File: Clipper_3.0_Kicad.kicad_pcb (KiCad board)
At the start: 2 copper layers, 19 parts, among them J10 Conn_01x19_Socket, J11 Screw_Terminal_01x02, J12 Conn_01x01_Socket, J13 Conn_01x01_Socket, J14 Conn_01x01_Socket, J15 Conn_01x01_Socket, J4 Conn_01x08_Socket, J5 Conn_01x08_Socket, J6 Conn_01x08_Socket, J9 Conn_01x19_Socket, U1 ESP32-DevKitC, U2 TB6612FNG_MODULE, U3 GY-521 MODULE, U4 DC/DC MINI-360

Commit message: Actualizacion de avance en SCH
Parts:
- removed REF**: TerminalBlock_Xinya_XY308-2.54-19P_1x19_P2.54mm_Horizontal, TerminalBlock:TerminalBlock_Xinya_XY308-2.54-19P_1x19_P2.54mm_Horizontal
- removed REF**: CP_Radial_D8.0mm_P3.50mm, Capacitor_THT:CP_Radial_D8.0mm_P3.50mm
- removed REF** (x2): TerminalBlock_Xinya_XY308-2.54-2P_1x02_P2.54mm_Horizontal, TerminalBlock:TerminalBlock_Xinya_XY308-2.54-2P_1x02_P2.54mm_Horizontal
- removed REF**: SOT-223-3_TabPin2, Package_TO_SOT_SMD:SOT-223-3_TabPin2
- added C1: C_Polarized_Small, Capacitor_THT:CP_Radial_D8.0mm_P3.50mm, F.Cu at (161.4, 65.0)
- added J20: Screw_Terminal_01x02, TerminalBlock:TerminalBlock_Xinya_XY308-2.54-2P_1x02_P2.54mm_Horizontal, F.Cu at (186.6, 63.7)
- added J21: Screw_Terminal_01x16, TerminalBlock:TerminalBlock_Xinya_XY308-2.54-16P_1x16_P2.54mm_Horizontal, F.Cu at (113.4, 76.1)
- added R1: 3.3K, Resistor_SMD:R_1206_3216Metric_Pad1.30x1.75mm_HandSolder, B.Cu at (122.2, 109.2)
- added R2: 4.7K, Resistor_SMD:R_1206_3216Metric_Pad1.30x1.75mm_HandSolder, B.Cu at (122.2, 111.9)
- added R3: 3.3V, Resistor_SMD:R_1206_3216Metric_Pad1.30x1.75mm_HandSolder, B.Cu at (147.9, 94.7)
- added R4: 4.7K, Resistor_SMD:R_1206_3216Metric_Pad1.30x1.75mm_HandSolder, B.Cu at (147.8, 98.0)
- U5: renamed from U1; value ESP32-DevKitC -> AMS1117-3.3; footprint Espressif:ESP32-DevKitC -> Package_TO_SOT_SMD:SOT-223-3_TabPin2; moved to B.Cu
- moved U5 64.7 mm to (164.5, 131.2)
- moved J10 50.0 mm to (127.8, 119.1), turned to 180 degrees
- moved J9 48.5 mm to (153.2, 119.1), turned to 180 degrees
- moved J11 18.7 mm to (184.0, 133.5)
- moved J6 17.8 mm to (170.6, 103.7), turned to 90 degrees
- moved J4 0.22 mm to (188.8, 86.6)
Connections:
- J10 pad 1: unconnected-(J10-Pin_1-Pad1) -> GND
- J10 pad 11: unconnected-(J10-Pin_11-Pad11) -> S1
- J10 pad 12: unconnected-(J10-Pin_12-Pad12) -> S0
- J10 pad 13: unconnected-(J10-Pin_13-Pad13) -> SIG
- J10 pad 17: unconnected-(J10-Pin_17-Pad17) -> Net-(J10-Pin_17)
- J10 pad 18: unconnected-(J10-Pin_18-Pad18) -> /LED
- J10 pad 19: unconnected-(J10-Pin_19-Pad19) -> /BTN
- J10 pad 2: unconnected-(J10-Pin_2-Pad2) -> Net-(J10-Pin_2)
- J10 pad 3: unconnected-(J10-Pin_3-Pad3) -> Net-(J10-Pin_3)
- J10 pad 6: unconnected-(J10-Pin_6-Pad6) -> Net-(J10-Pin_6)
- J10 pad 7: unconnected-(J10-Pin_7-Pad7) -> GND
- J10 pad 8: unconnected-(J10-Pin_8-Pad8) -> S3
- J10 pad 9: unconnected-(J10-Pin_9-Pad9) -> S2
- J11 pad 1: unconnected-(J11-Pin_1-Pad1) -> /BO2
- J11 pad 2: unconnected-(J11-Pin_2-Pad2) -> /BO1
- J12 pad 1: unconnected-(J12-Pin_1-Pad1) -> VCC12V
- J13 pad 1: unconnected-(J13-Pin_1-Pad1) -> GND
- J14 pad 1: unconnected-(J14-Pin_1-Pad1) -> VCC5V
- J15 pad 1: unconnected-(J15-Pin_1-Pad1) -> GND
- J5 pad 1: /VM -> VCC12V
- J5 pad 2: /VCC -> VCC3.3V
- J6 pad 1: unconnected-(J6-Pin_1-Pad1) -> VCC3.3V
- J6 pad 2: unconnected-(J6-Pin_2-Pad2) -> GND
- J6 pad 3: unconnected-(J6-Pin_3-Pad3) -> Net-(J10-Pin_3)
- J6 pad 4: unconnected-(J6-Pin_4-Pad4) -> Net-(J10-Pin_6)
- J9 pad 10: unconnected-(J9-Pin_10-Pad10) -> /BIN1
- J9 pad 11: unconnected-(J9-Pin_11-Pad11) -> /STBY
- J9 pad 12: unconnected-(J9-Pin_12-Pad12) -> /AIN1
- J9 pad 13: unconnected-(J9-Pin_13-Pad13) -> /AIN2
- J9 pad 14: unconnected-(J9-Pin_14-Pad14) -> GND
- J9 pad 15: unconnected-(J9-Pin_15-Pad15) -> /PWMA
- J9 pad 19: unconnected-(J9-Pin_19-Pad19) -> VCC5V
- J9 pad 7: unconnected-(J9-Pin_7-Pad7) -> Net-(J9-Pin_7)
- J9 pad 8: unconnected-(J9-Pin_8-Pad8) -> /PWMB
- J9 pad 9: unconnected-(J9-Pin_9-Pad9) -> /BIN2
- U5 pad 1: unconnected-(U1-3V3-Pad1) -> GND
- U5 pad 2: unconnected-(U1-CHIP_PU-Pad2) -> VCC3.3V
- U5 pad 3: unconnected-(U1-SENSOR_VP/GPIO36/ADC1_CH0-Pad3) -> VCC5V
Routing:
- net VCC3.3V: track 0.00 -> 191.0 mm
- net VCC5V: track 0.00 -> 158.0 mm
- net unconnected-(U4-VCC_In-Pad1): track 151.1 -> 0.00 mm, vias 2 -> 0
- net VCC12V: track 0.00 -> 149.7 mm
- net /BO2: track 0.00 -> 120.2 mm
- net Net-(J2-Pin_7): track 120.0 -> 0.00 mm
- net Net-(J2-Pin_6): track 106.0 -> 0.00 mm
- net unconnected-(U3-VCC-Pad1): track 105.8 -> 0.00 mm
- net /BO1: track 0.00 -> 105.7 mm
- net Net-(J10-Pin_6): track 0.00 -> 89.3 mm
- net Net-(J10-Pin_3): track 0.00 -> 79.7 mm
- net Net-(J2-Pin_2): track 66.1 -> 0.00 mm
- net /ENCD: track 0.00 -> 62.3 mm
- net /PWMA: track 0.00 -> 44.2 mm
- net GND: track 22.5 -> 66.6 mm, vias 5 -> 7
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
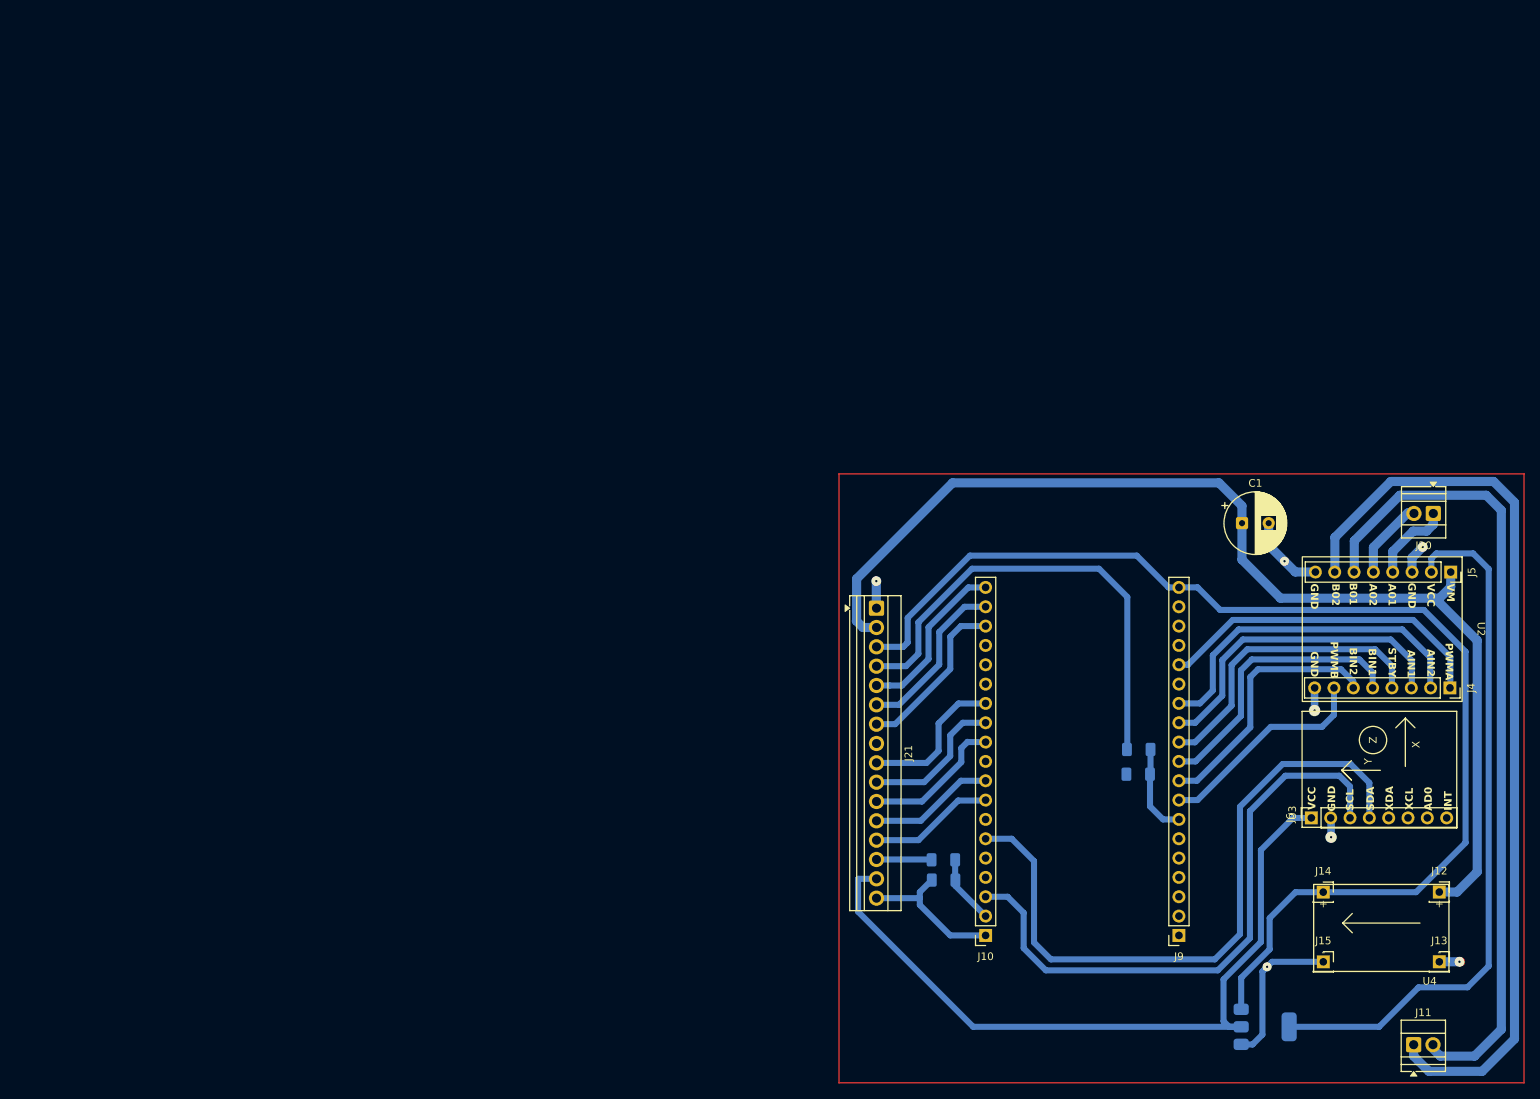
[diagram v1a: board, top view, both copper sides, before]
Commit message: Terminacion del equematico y redistribucion de pines del ESP32 para evitar conflicto con wifi
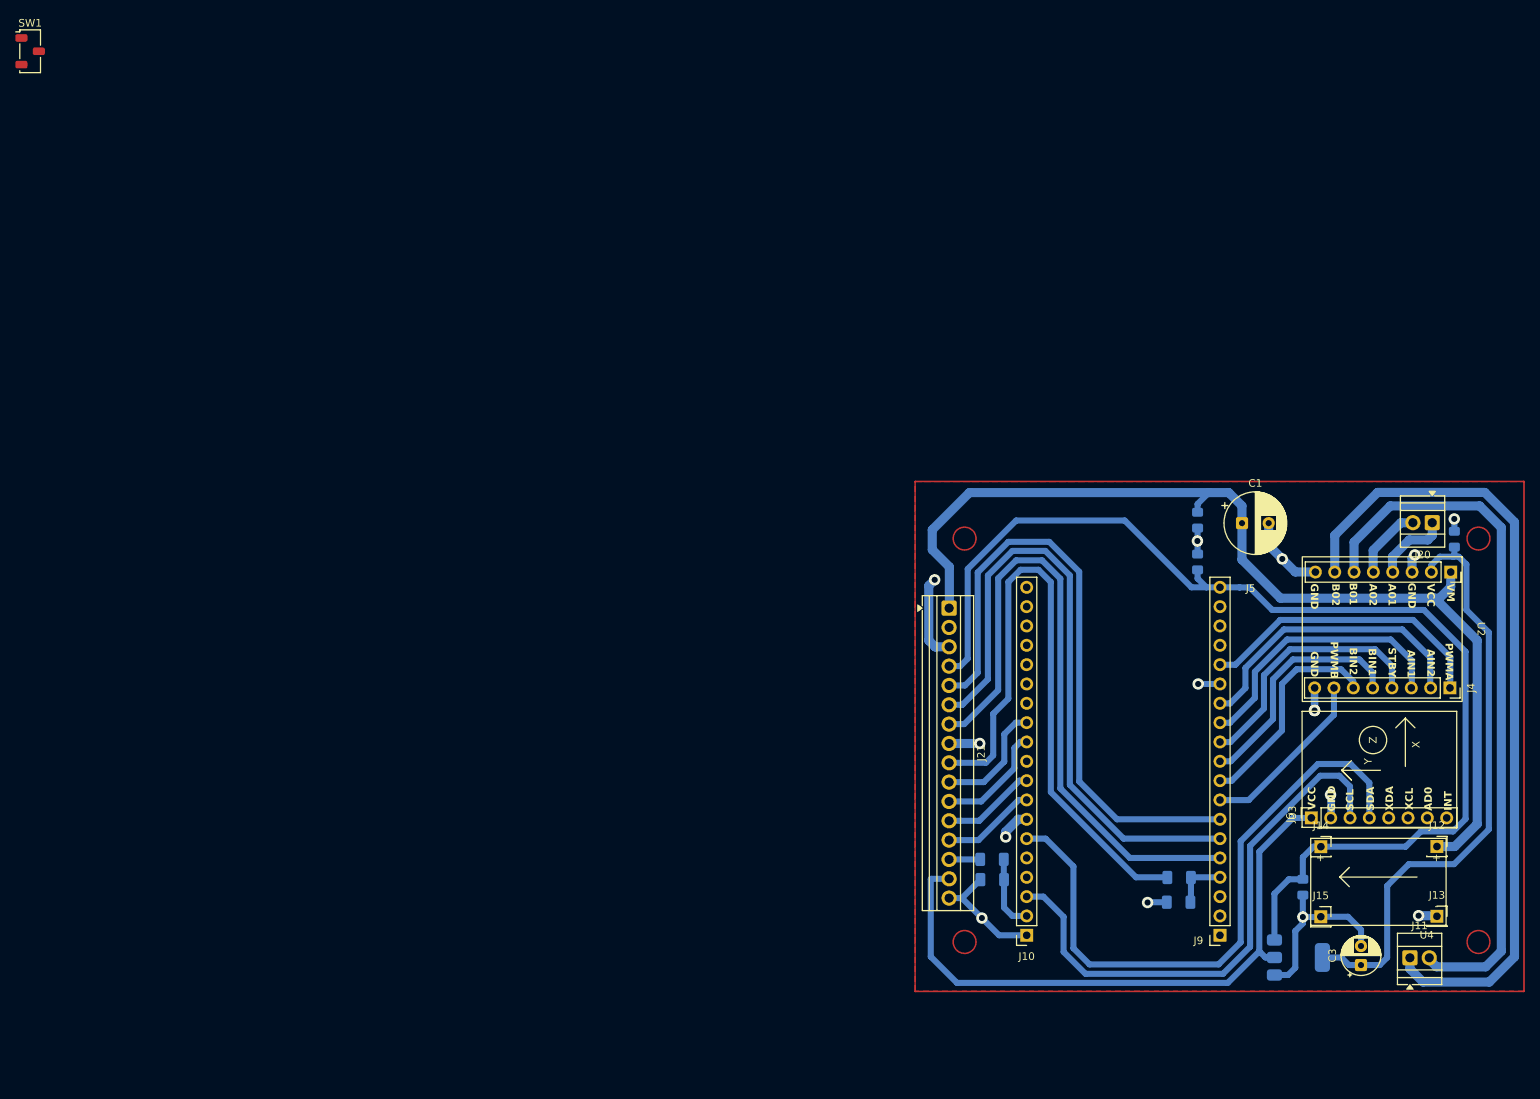
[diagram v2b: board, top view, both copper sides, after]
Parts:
- added C2: 0.1uF, Capacitor_SMD:C_0805_2012Metric_Pad1.18x1.45mm_HandSolder, B.Cu at (155.6, 64.6)
- added C3: 22uF, Capacitor_THT:CP_Radial_D5.0mm_P2.50mm, F.Cu at (177.1, 123.0)
- added C4: 0.1uF, Capacitor_SMD:C_0805_2012Metric_Pad1.18x1.45mm_HandSolder, B.Cu at (169.4, 112.8)
- added C5: 0.1uF, Capacitor_SMD:C_0805_2012Metric_Pad1.18x1.45mm_HandSolder, B.Cu at (189.3, 67.1)
- added C6: 0.1uF, Capacitor_SMD:C_0805_2012Metric_Pad1.18x1.45mm_HandSolder, B.Cu at (155.6, 70.1)
- added SW1: SW_Nidec_CAS-120A1, Button_Switch_SMD:Nidec_Copal_CAS-120A, F.Cu at (2.23, 2.98)
- C1: value C_Polarized_Small -> 470uF
- R3: value 3.3V -> 3.3K
- U4: value DC/DC MINI-360 -> DC/DC Mini360
- moved R3 17.6 mm to (153.2, 111.5)
- moved R4 17.6 mm to (153.1, 114.8)
- moved J11 11.4 mm to (183.5, 122.1)
- moved U5 10.1 mm to (168.9, 122.0)
- moved J21 9.54 mm to (123.0, 76.1)
- moved R1 6.39 mm to (128.6, 109.2)
- moved R2 6.39 mm to (128.6, 111.8)
- moved U4 6.07 mm to (187.0, 116.5)
- moved J12 5.99 mm to (187.1, 107.5)
- moved J13 5.99 mm to (187.1, 116.6)
- moved J14 5.99 mm to (171.8, 107.5)
- moved J15 5.93 mm to (171.8, 116.7)
- moved J9 5.40 mm to (158.6, 119.1)
- moved J10 5.40 mm to (133.2, 119.1)
- moved J20 1.22 mm to (186.4, 64.9)
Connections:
- net Net-(J10-Pin_3) renamed /SCL
- net Net-(J10-Pin_6) renamed /SDA
- J10 pad 13: SIG -> unconnected-(J10-Pin_13-Pad13)
- J10 pad 17: Net-(J10-Pin_17) -> unconnected-(J10-Pin_17-Pad17)
- J10 pad 18: /LED -> unconnected-(J10-Pin_18-Pad18)
- J10 pad 19: /BTN -> unconnected-(J10-Pin_19-Pad19)
- J10 pad 2: Net-(J10-Pin_2) -> ENCI
- J21 pad 1: GND -> VCC12V
- J21 pad 14: /ENCI -> ENCI
- J21 pad 2: VCC12V -> VCC12VBat
- J21 pad 3: VCC5V -> GND
- J21 pad 4: /ENCD -> VCC5V
- J21 pad 5: /BTN -> LED
- J21 pad 6: /LED -> BTN
- J21 pad 7: Net-(J10-Pin_17) -> SIG
- J21 pad 9: SIG -> ENCD
- J9 pad 4: unconnected-(J9-Pin_4-Pad4) -> ENCD
- J9 pad 5: unconnected-(J9-Pin_5-Pad5) -> SIG
- J9 pad 6: unconnected-(J9-Pin_6-Pad6) -> BTN
- J9 pad 7: Net-(J9-Pin_7) -> LED
- R1 pad 1: /ENCI -> ENCI
- R1 pad 2: Net-(J10-Pin_2) -> ENCI
- R2 pad 1: Net-(J10-Pin_2) -> ENCI
- R3 pad 1: /ENCD -> ENCD
- R3 pad 2: Net-(J9-Pin_7) -> ENCD
- R4 pad 1: Net-(J9-Pin_7) -> ENCD
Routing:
- net ENCD: track 0.00 -> 91.5 mm
- net BTN: track 0.00 -> 83.7 mm
- net LED: track 0.00 -> 82.4 mm
- net SIG: track 19.7 -> 85.7 mm
- net /ENCD: track 62.3 -> 0.00 mm
- net VCC3.3V: track 191.0 -> 162.0 mm
- net GND: track 66.6 -> 90.8 mm, vias 7 -> 15
- net /LED: track 22.2 -> 0.00 mm
- net Net-(J10-Pin_17): track 22.2 -> 0.00 mm
- net /BTN: track 22.1 -> 0.00 mm
- net ENCI: track 0.00 -> 13.9 mm
- net VCC12V: track 149.7 -> 136.0 mm
- net /BO2: track 120.2 -> 106.8 mm
- net /BO1: track 105.7 -> 92.8 mm
- net Net-(J9-Pin_7): track 12.0 -> 0.00 mm
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- added copper zone on F.Cu, net GND
